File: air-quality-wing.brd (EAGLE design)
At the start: 55.9 x 33 mm, 37 parts, among them J1 CON-0024, Q1 TR-0001, Q2 TR-0001, Q3 TR-0003, U1 POWER-VREG-FB-EN-SW-350MA, U2 CCS811B-JOPD500, U3 POWER-SWITCH-SIP32509DT, U4 SI7021-A20-GM1R

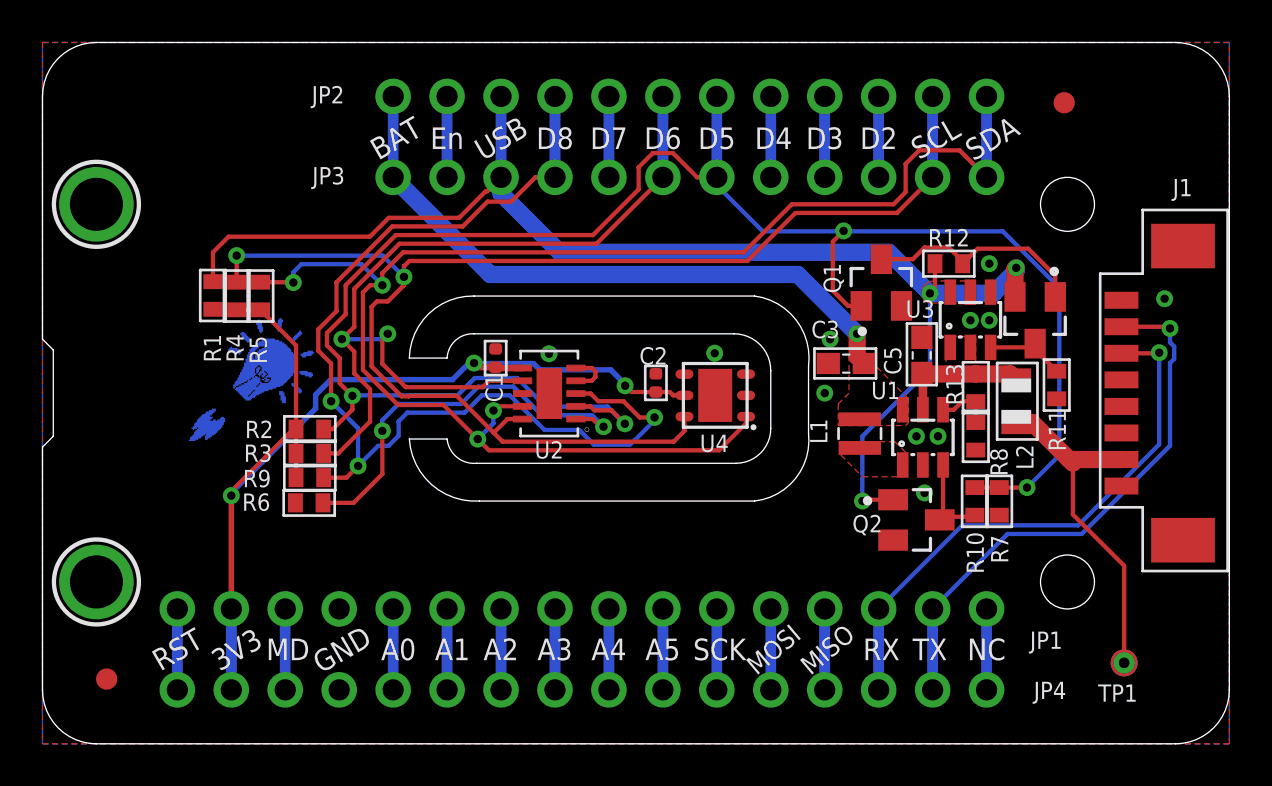
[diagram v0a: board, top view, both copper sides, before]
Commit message: Committing v6 changes:
Changed:

* Formfactor to standard Feather size
* Replaced temperature/humidity sensor with SHTC3
* Replaced TVOC sensor with SGP40
* Changed MCP1640 package to DSON from SOT23-5
* Hatched ground planes on both top and bottom
* Re-designed sensor placement
* Thermal isolation slots for SHTC3
* Pinout for PM2.5 connector reverted back to original design (allows for bidirectional use of cable)

Added:

* Added I2C power control to D4
* Added battery backpack (CR2 holder)
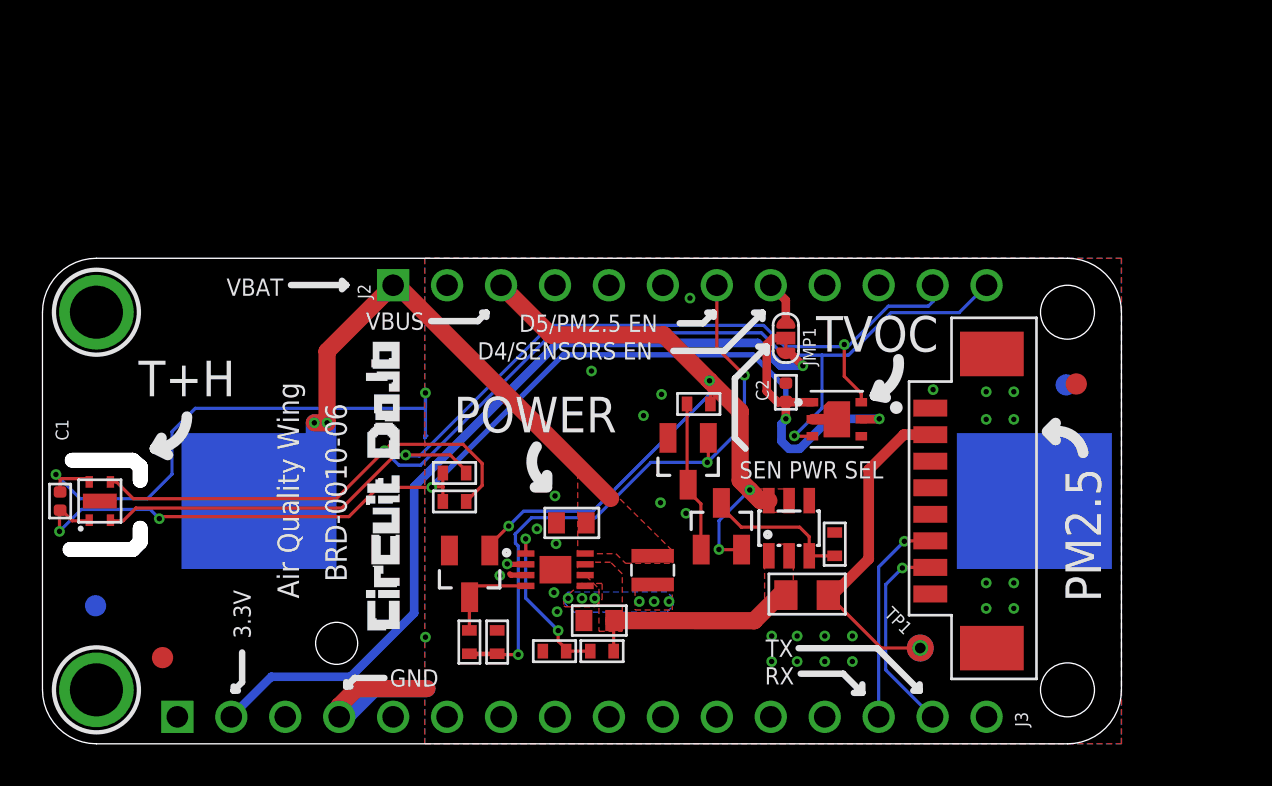
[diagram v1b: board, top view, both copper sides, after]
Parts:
- removed JP1, JP4: (no value), microbuilder:1X16_ROUND
- removed JP2, JP3: (no value), microbuilder:1X12_ROUND
- removed L2: 2k, wolff-den:R0805
- removed R1, R6, R9: 100k, wolff-den:R0402
- removed R4, R5: 20k, wolff-den:R0402
- removed U4: SI7021-A20-GM1R, wolff-den:SON100P300X300X80-7N
- added FB1: 2k, wolff-den:R0805
- added J2: CON-HEADER-1X12-PPPC121LFBN-RC, wolff-den:CON-HEADER-1X12
- added J3: CON-HEADER-1X16-PPPC161LFBN-RC, wolff-den:CON-HEADER-1X16
- added JMP1: JUMPER-3/1, wolff-den:JUMPER-ROUND-3-NO-R
- added PAD1: BH-CR2-1010, wolff-den:1010
- added SOLDER1: SOLDER, wolff-den:PLACEHOLDER
- added U$1: (no value), SparkFun-Aesthetics:OSHW-LOGO-S
- added U$2: (no value), wolff-den:LOGO-CIRCUITDOJO
- added U$3, U$4: FIDUCIAL-1MM, wolff-den:FIDUCIAL-1MM
- added U$5: (no value), wolff-den:BACKPACK
- added U$6: (no value), frames:A3L-LOC
- added U6: IC-SHTC3, wolff-den:IC-SHTC3
- PCB1: value PCB-PS-CCS811-SI7021 -> PCB-PS-AQW
- Q3: device wolff-den:SOT23 -> wolff-den:SOT23@1
- R10, R12, R13, R7, R8: device wolff-den:R0402 -> wolff-den:R0402-M
- R11: value 1k -> 100k; device wolff-den:R0402 -> wolff-den:R0402-M
- R2, R3: value 100k -> 20k; device wolff-den:R0402 -> wolff-den:R0402-M
- U$31, U$32: value MOUNTINGHOLE2.5 -> MOUNTING-HOLE-2.5MM-PLATED; device microbuilder:MOUNTINGHOLE_2.5_PLATED -> wolff-den:MOUNTING-HOLE-2.5MM-PLATED
- U$34, U$35: value FIDUCIAL"" -> FIDUCIAL-1MM; device microbuilder:FIDUCIAL_1MM -> wolff-den:FIDUCIAL-1MM
- U1: value POWER-VREG-FB-EN-SW-350MA -> POWER-VREG-FB-EN-SW-350MA-DFN8; device wolff-den:SOT23-6 -> wolff-den:DFN200X300X100-9N
- U2: value CCS811B-JOPD500 -> IC-SGP40; device wolff-den:SON60P400X270X110-11N -> wolff-den:XDCR_SGP30-2.5K
- U3: value POWER-SWITCH-SIP32509DT -> POWER-SWITCH-SIP32509-SO23-6
- moved R10 24.7 mm to (20.1, 4.79), turned to 270 degrees
- moved R7 24.5 mm to (21.4, 4.79), turned to 270 degrees
- moved R8 22.3 mm to (24.1, 4.36), turned to 0 degrees
- moved C1 21.6 mm to (0.83, 11.4)
- moved R13 21.5 mm to (26.3, 4.36), turned to 0 degrees
- moved Q2 21.2 mm to (20.1, 8.00), turned to 180 degrees
- moved C5 19.7 mm to (26.2, 5.80), turned to 180 degrees
- moved U1 18.4 mm to (24.2, 8.20)
- moved Q3 17.7 mm to (32.0, 10.2), turned to 0 degrees
- moved C3 15.0 mm to (24.9, 10.4)
- moved U2 13.6 mm to (37.4, 15.3), turned to 0 degrees
- moved R12 13.5 mm to (30.9, 16.0), turned to 0 degrees
- moved U$35 13.3 mm to (48.7, 16.9)
- moved U3 13.0 mm to (35.1, 10.2)
- moved R11 12.9 mm to (37.3, 9.40), turned to 270 degrees
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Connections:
- net N$3 renamed Q1_D
- net N$7 renamed LOAD_SW_EN
- removed net D4: JP2.8, JP3.8
- removed net D5: JP2.7, JP3.7, Q1.1, R10.2, R2.1, R7.2, U2.2
- removed net N$1: L1.P$1, U1.1
- removed net N$4: R9.2, U2.1
- removed net N$5: U2.4, U2.5
- removed net N$6: Q2.3, R10.1, U1.3
- new net D4/SENSORS_VCC: J2.8, JMP1.P$1
- new net D5/HPMA_EN: J2.7, Q1.1, R10.2, R7.2
- new net SENSORS_VCC: C1.1, C2.1, JMP1.P$2, R2.2, R3.2, U2.1, U2.5, U6.1
- new net V5V0_EN: Q2.3, R10.1, U1.4
- new net V5V0_SW: L1.P$1, U1.5
- net !RESET: now also J3.1; no longer JP1.16, JP4.16
- net +3V3: now also J3.2, JMP1.P$3; no longer C1.1, C2.1, JP1.15, JP4.15, R2.2, R3.2, R4.2, R5.2, R6.2, U2.6, U4.5
- net A0: now also J3.5; no longer JP1.12, JP4.12
- net A1: now also J3.6; no longer JP1.11, JP4.11
- net A2: now also J3.7; no longer JP1.10, JP4.10
- net A3: now also J3.8; no longer JP1.9, JP4.9
- net A4: now also J3.9; no longer JP1.8, JP4.8
- net A5: now also J3.10; no longer JP1.7, JP4.7
- net D2: now also J2.10; no longer JP2.10, JP3.10
- net D3: now also J2.9; no longer JP2.9, JP3.9
- net D6: now also J2.6; no longer JP2.6, JP3.6, R3.1, U2.7
- net D7: now also J2.5; no longer JP2.5, JP3.5
- net D8: now also J2.4; no longer JP2.4, JP3.4, R6.1, U2.3
- net EN: now also J2.2; no longer JP2.2, JP3.2
- net GND: now also J1.8, J3.4, PAD1.P$2, U1.3, U1.9, U2.2, U2.4, U2.7, U6.4; no longer J1.1, JP1.13, JP4.13, R1.1, R9.1, U2.11, U4.2, U4.7
- net MD: now also J3.3; no longer JP1.14, JP4.14
- net MISO: now also J3.13; no longer JP1.4, JP4.4
- net MOSI: now also J3.12; no longer JP1.5, JP4.5
- net N$2: now also U1.1; no longer U1.4
- net NC: now also J3.16; no longer JP1.1, JP4.1
- net RX: now also J1.6, J3.14; no longer J1.3, JP1.3, JP4.3
- net SCK: now also J3.11; no longer JP1.6, JP4.6
- net SCL: now also J2.11, R2.1, U2.6, U6.2; no longer JP2.11, JP3.11, R4.1, U2.10, U4.6
- net SDA: now also J2.12, R3.1, U2.3, U6.3; no longer JP2.12, JP3.12, R5.1, U2.9, U4.1
- net TX: now also J1.7, J3.15; no longer J1.2, JP1.2, JP4.2
- net V5V0_BEAD: now also FB1.1, U1.6, U1.7; no longer L2.1, U1.5
- net V5V0_HAT: now also FB1.2, J1.2; no longer J1.7, L2.2
- net VBAT: now also J2.1, PAD1.P$1, U1.8; no longer JP2.1, JP3.1, U1.6
- net VBUS: now also J2.3; no longer JP2.3, JP3.3, R1.2
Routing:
- net D5: track 85.8 -> 0.00 mm, vias 4 -> 0
- net SENSORS_VCC: track 0.00 -> 58.4 mm, vias 0 -> 5
- net D8: track 49.4 -> 0.00 mm, vias 3 -> 0
- net D6: track 41.3 -> 0.00 mm, vias 2 -> 0
- net GND: track 0.00 -> 38.6 mm, vias 11 -> 33
- net D5/HPMA_EN: track 0.00 -> 30.6 mm, vias 0 -> 3
- net VBUS: track 63.2 -> 38.5 mm, vias 3 -> 4
- net N$4: track 19.2 -> 0.00 mm, vias 2 -> 0
- net TX: track 26.2 -> 9.58 mm
- net RX: track 26.3 -> 10.00 mm
- net SCL: track 64.4 -> 51.2 mm
- net SDA: track 71.6 -> 59.6 mm, vias 4 -> 2
- net +3V3: track 50.8 -> 39.2 mm, vias 3 -> 1
- net N$2: track 2.70 -> 7.91 mm, vias 0 -> 2
- net V5V0_EN: track 0.00 -> 4.67 mm
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- added copper zone on layer 1, net V5V0_SW
- added copper zone on layer 16, net V5V0_SW
- removed copper zone on layer 1, net N$1
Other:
- board size 55.9 x 33 mm -> 50.8 x 22.9 mm
- board text added: "(Top down)"
- board text added: "3.3V"
- board text added: "Air Quality Wing"
- board text added: "Air Quality Wing V6"
- board text added: "BATTERY BACKPACK"
- board text added: "BOT"
- board text added: "BRD-0010-06"
- board text added: "Confidential - Property of Circuit Dojo LLC"
- board text added: "D4/SENSORS EN"
- board text added: "D5/PM2.5 EN"
- board text added: "Notes: * T4 solder paste * Lead Free assembly * Measures in mm"
- board text added: "PM2.5"
- board text added: "POWER"
- board text added: "SEN PWR SEL"
- board text added: "T+H"
- board text added: "TOP"
- board text added: "TVOC"
- board text added: "VBAT"
- board text added: "VBUS"
- board text removed: "2"
- board text removed: "3V3"
- board text removed: "A0"
- board text removed: "A1"
- board text removed: "A2"
- board text removed: "A3"
- board text removed: "A4"
- board text removed: "A5"
- board text removed: "BAT"
- board text removed: "BRD-0010-03"
- board text removed: "D2"
- board text removed: "D3"
- board text removed: "D4"
- board text removed: "D5"
- board text removed: "D6"
- board text removed: "D7"
- board text removed: "D8"
- board text removed: "En"
- board text removed: "MD"
- board text removed: "MISO"
- board text removed: "MOSI"
- board text removed: "NC"
- board text removed: "Particle"
- board text removed: "RST"
- board text removed: "SCK"
- board text removed: "SCL"
- board text removed: "SDA"
- board text removed: "USB"
